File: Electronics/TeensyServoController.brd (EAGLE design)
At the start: 50.8 x 38.1 mm, 17 parts, among them U1 MK20DX128VLH5, U2 AP3211_SWITCHING_REGULATOR, U3 AP3211_SWITCHING_REGULATOR, U4 AP3211_SWITCHING_REGULATOR

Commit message: Continued Work on Teensy servo controller
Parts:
- added C1, C5, C6: 10nF, resistor:C0402
- added C10, C11, C12, C14, C15, C16, C7, C8: 0.1uF, resistor:C0402
- added C13, C9: 2.2uF, resistor:C0603
- added C2, C3, C4: 10uF, resistor:C0805
- added Q1: 16MHz, crystal:CTS406
- added R1, R3, R4: 349k, resistor:R0402
- added R2, R5, R6: 49.9k, resistor:R0402
- added R7, R8: 33, resistor:R0402
- added R9: 470, resistor:R0402
- added U5: (no value), SparkFun-Connectors:USB-AB-MICRO-SMD
- moved U$3 21.8 mm to (43.3, 30.7), turned to 270 degrees
- moved U1 8.47 mm to (32.3, 15.5), turned to 90 degrees
- moved U4 5.64 mm to (22.1, 30.0)
- moved U3 4.68 mm to (22.1, 18.8)
- moved U2 4.52 mm to (22.1, 7.62)
- moved L2 3.98 mm to (18.3, 19.1)
- moved L1 3.98 mm to (18.3, 7.87)
- moved L3 3.87 mm to (18.3, 30.2)
- moved JP9 3.56 mm to (1.52, 33.0)
- moved JP4 3.56 mm to (1.52, 16.3)
- moved JP5 3.56 mm to (1.52, 19.1)
- moved JP6 3.56 mm to (1.52, 21.8)
- moved JP1 3.56 mm to (1.52, 5.08)
- moved JP2 3.56 mm to (1.52, 7.87)
- moved JP3 3.56 mm to (1.52, 10.7)
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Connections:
- removed net N$8: U$3.17, U$3.25, U$3.47
- new net N$10: R7.1, U5.D-
- new net N$14: C1.2, U2.1
- new net N$15: R8.2, U1.5
- new net N$16: R4.1, R6.2, U4.3
- new net N$17: C5.2, U3.1
- new net N$18: R3.1, R5.2, U3.3
- new net N$19: C6.2, U4.1
- new net N$20: C6.1, L3.P$1, R4.2, U4.6
- new net N$21: C14.1, Q1.3, U1.32
- new net N$22: C15.1, Q1.1, U1.33
- new net N$23: C16.2, U1.8
- new net N$24: C9.1, R9.1, U1.13
- new net N$25: C7.2, C8.2, C9.2, U1.15, U1.16
- new net N$26: C7.1, U1.17
- new net N$27: C8.1, R9.2, U1.14
- new net N$30: U$3.8, U1.34
- new net N$31: C10.1, C11.1, C12.1, C13.1, U$3.42, U$3.43, U1.3, U1.30, U1.48, U1.7
- new net N$6: R1.1, R2.2, U2.3
- new net N$9: R8.1, U5.D+
- net GND: now also C10.2, C11.2, C12.2, C13.2, C14.2, C15.2, C16.1, C2.2, C3.2, C4.2, R2.1, R5.1, R6.1, U$3.17, U$3.25, U$3.47, U$3.5, U1.31, U1.4, U1.47, U2.2, U3.2, U4.2, U5.GND
- net N$1: now also U5.ID
- net N$11: now also C5.1, R3.2
- net N$12: now also R7.2, U1.6; no longer L3.P$1, U4.6
- net N$13: now also C1.1, R1.2
- net VCC: now also C2.1, C3.1, C4.1
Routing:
- net GND: track 0.00 -> 10.6 mm, vias 0 -> 25
- net N$13: track 0.00 -> 7.80 mm
- net N$11: track 0.00 -> 7.51 mm
- net N$20: track 0.00 -> 7.51 mm
- net VCC: track 0.00 -> 5.24 mm
- net N$6: track 0.00 -> 3.07 mm
- net N$18: track 0.00 -> 3.07 mm
- net N$16: track 0.00 -> 3.07 mm
- net N$17: track 0.00 -> 2.45 mm
- net N$14: track 0.00 -> 2.45 mm
- net N$19: track 0.00 -> 2.45 mm
- net N$9: track 0.00 -> 2.45 mm
- net N$10: track 0.00 -> 2.44 mm
- added copper zone on layer 1, net GND
- added copper zone on layer 16, net GND
- added copper zone on layer 1, net N$11
- added copper zone on layer 1, net N$13
- added copper zone on layer 1, net N$20
- added copper zone on layer 1, net SERVO_VDD-1
- added copper zone on layer 1, net SERVO_VDD-2
- added copper zone on layer 1, net SERVO_VDD-3

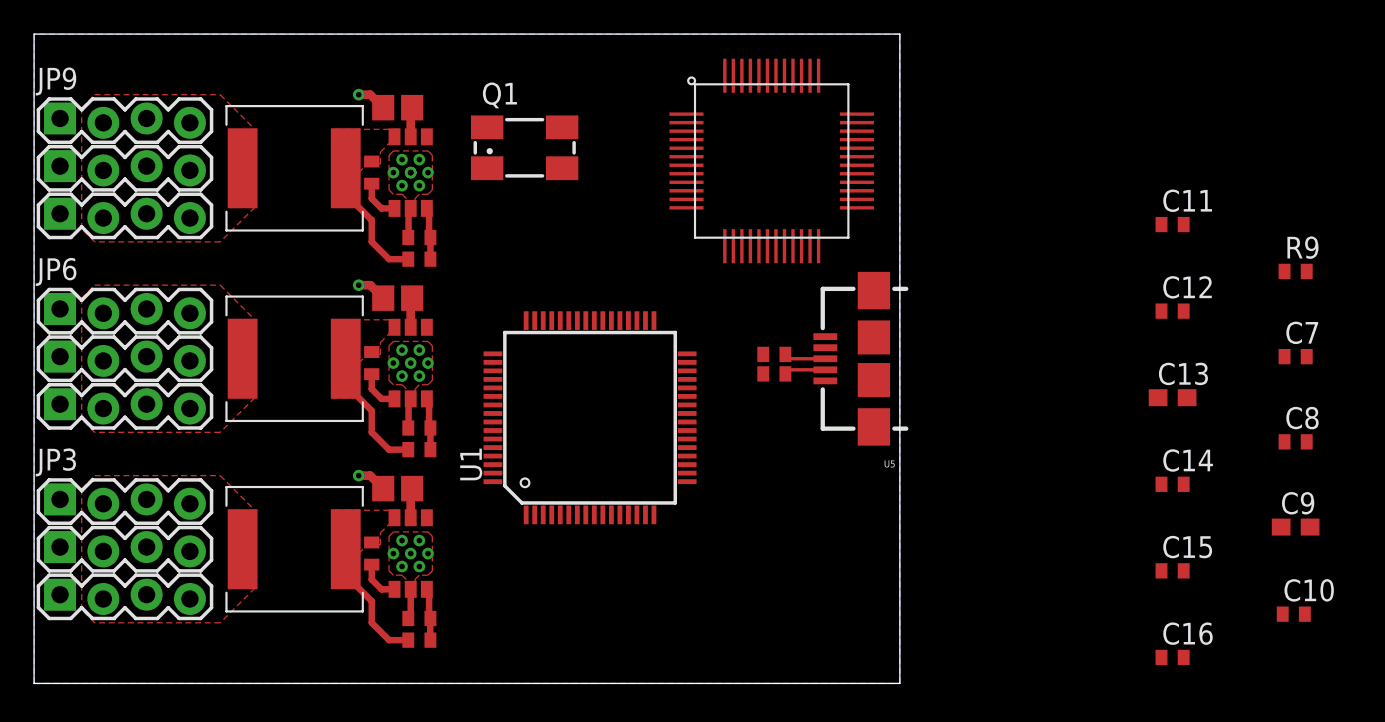
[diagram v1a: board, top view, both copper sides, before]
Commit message: Servo controller mostly done (no I sense)
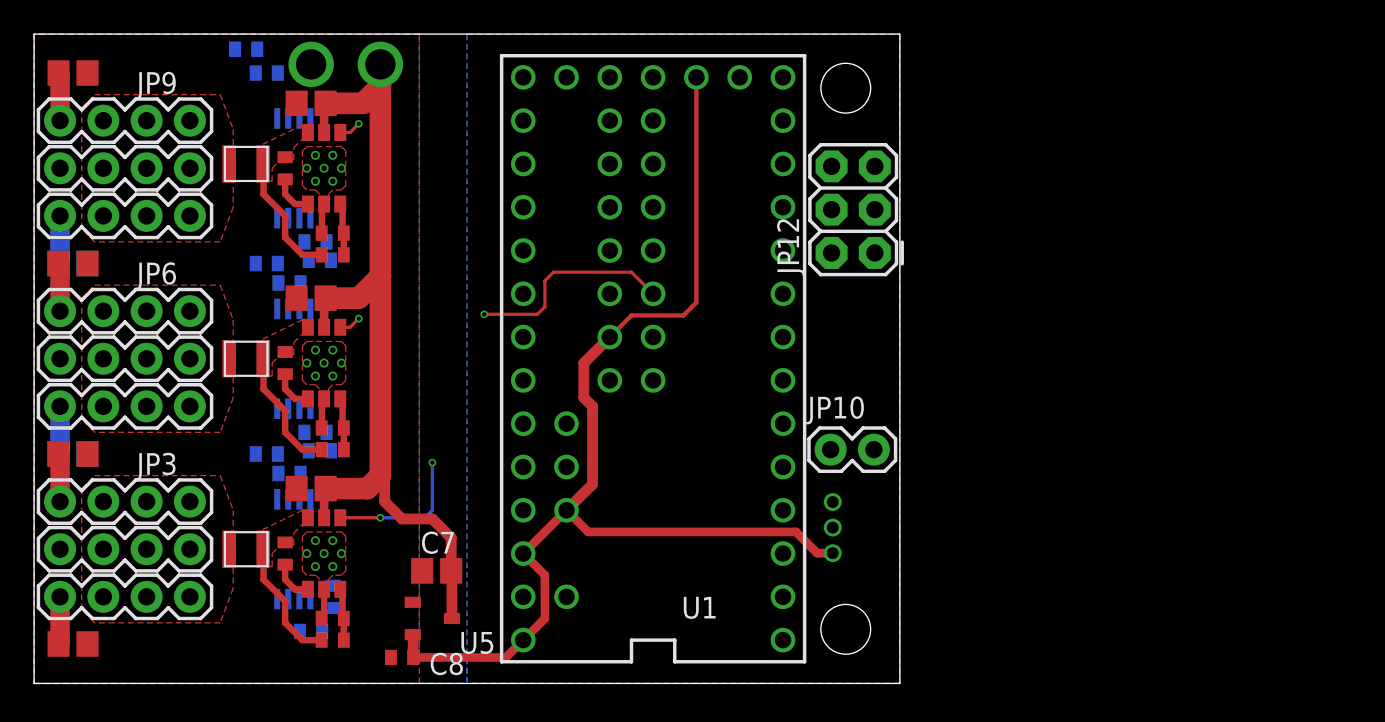
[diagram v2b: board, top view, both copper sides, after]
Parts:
- removed C10, C11, C12, C14, C15, C16: 0.1uF, resistor:C0402
- removed C13, C9: 2.2uF, resistor:C0603
- removed Q1: 16MHz, crystal:CTS406
- removed U$3: MINI54TAN, TeensyCustom:MINI54TAN
- added JP10: (no value), SparkFun-Connectors:1X02
- added JP11: 3-PIN_JST_ZH_PTH_CONNECTORRIGHT_ANGLE_PTH, My Parts:3-PIN_JST_ZH_CONNECTOR_TH
- added JP12: (no value), SparkFun-Connectors:2X3
- added R10, R11, R12, R17, R20, R23: 1k, resistor:R0402
- added R13, R14, R15, R18, R21, R24: 63.4k, resistor:R0402
- added R16, R19, R22: 0.1, resistor:R0805
- added U6, U7, U8: MCP6L02T-E/MS, linear:TSSOP8
- C7: value 0.1uF -> 10uF; device resistor:C0402 -> resistor:C0805
- JP1, JP2, JP3, JP4, JP5, JP6, JP7, JP8, JP9: device SparkFun-Connectors:1X04_LOCK -> SparkFun-Connectors:1X04
- L1, L2, L3: device SparkFun-Passives:CR75 -> inductors:1008
- R7, R8: value 33 -> 0.1; device resistor:R0402 -> resistor:R0805
- R9: value 470 -> 0.1; device resistor:R0402 -> resistor:R0805
- U1: value MK20DX128VLH5 -> TEENSY_3.1_ALLPINS; device TeensyCustom:MK20DX128VLH5 -> Teensy3.0:TEENSY_3.0_ALLPINS
- U2, U3, U4: value AP3211_SWITCHING_REGULATOR -> AP3211KTR-G1
- U5: value (none) -> AP2210N-3.3TRG1; device SparkFun-Connectors:USB-AB-MICRO-SMD -> My Parts:SOT23
- moved R9 72.5 mm to (2.29, 13.5), flipped to the bottom
- moved C8 53.9 mm to (21.6, 1.52), turned to 180 degrees
- moved C7 51.9 mm to (23.6, 6.60), turned to 180 degrees
- moved R7 44.1 mm to (2.29, 2.31)
- moved R8 41.6 mm to (2.29, 13.5)
- moved U5 30.1 mm to (23.4, 3.81), turned to 270 degrees
- moved L3 5.85 mm to (12.4, 30.5)
- moved L1 5.84 mm to (12.4, 7.87)
- moved L2 5.84 mm to (12.4, 19.1)
- moved U1 5.40 mm to (36.3, 19.1), turned to 180 degrees
- moved C6 5.09 mm to (14.7, 30.2)
- moved R4 5.09 mm to (17.5, 25.1)
- moved R6 5.09 mm to (17.5, 26.4)
- moved C4 5.09 mm to (16.3, 34.0)
- moved U4 5.09 mm to (17.0, 30.2)
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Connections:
- removed net N$1: U$3.38, U1.23, U5.ID
- removed net N$12: R7.2, U1.6
- removed net N$15: R8.2, U1.5
- removed net N$21: C14.1, Q1.3, U1.32
- removed net N$22: C15.1, Q1.1, U1.33
- removed net N$23: C16.2, U1.8
- removed net N$24: C9.1, R9.1, U1.13
- removed net N$25: C7.2, C8.2, C9.2, U1.15, U1.16
- removed net N$26: C7.1, U1.17
- removed net N$27: C8.1, R9.2, U1.14
- removed net N$30: U$3.8, U1.34
- removed net N$31: C10.1, C11.1, C12.1, C13.1, U$3.42, U$3.43, U1.3, U1.30, U1.48, U1.7
- removed net N$4: U$3.37, U1.24
- new net CS0: JP12.3, U1.10
- new net CURRENT-1: JP1.1, R7.2, U6.3
- new net CURRENT-3: JP3.1, R8.2, U6.5
- new net CURRENT-4: JP4.1, R9.2, U7.3
- new net CURRENT-6: JP6.1, R16.2, U7.5
- new net CURRENT-7: JP7.1, R19.2, U8.3
- new net CURRENT-9: JP9.1, R22.2, U8.5
- new net EN-1: U1.33, U2.4
- new net EN-2: U1.24, U3.4
- new net EN-3: U1.32, U4.4
- new net MISO/MOSI: JP12.5, U1.12
- new net MOSI/MISO: JP12.6, U1.11
- new net SAT-RX: JP10.1, JP11.P$3, U1.0
- new net SCLK: JP12.4, U1.13
- new net SENSE-1: R13.2, U6.1
- new net SENSE-3: R14.2, U6.7
- new net SENSE-4: R15.2, U7.1
- new net SENSE-6: R18.2, U7.7
- new net SENSE-7: R21.2, U8.1
- new net SENSE-9: R24.2, U8.7
- new net VBAT: U1.VBAT
- new net VDD: C8.1, JP11.P$1, U1.3.3V, U1.3.3V1, U1.3.3V2, U1.AREF, U1.VIN, U5.P$2, U6.8, U7.8, U8.8
- new net VUSB: U1.VUSB
- net ANALOG-1: now also U1.22/A8
- net ANALOG-2: now also U1.21/A7
- net ANALOG-3: now also U1.20/A6
- net ANALOG-4: now also U1.19/A5
- net ANALOG-5: now also U1.18/A4
- net ANALOG-6: now also U1.17/A3
- net ANALOG-7: now also U1.16/A2
- net ANALOG-8: now also U1.15/A1
- net ANALOG-9: now also U1.14/A0
- net GND: now also C7.2, C8.2, JP10.2, JP11.P$2, JP12.1, R10.2, R11.2, R12.2, R16.1, R17.2, R19.1, R20.2, R22.1, R23.2, R7.1, R8.1, R9.1, U1.AGND, U1.GND, U1.GND1, U1.GND2, U5.P$1, U6.4, U7.4, U8.4; no longer C10.2, C11.2, C12.2, C13.2, C14.2, C15.2, C16.1, JP1.1, JP3.1, JP4.1, JP6.1, JP7.1, JP9.1, U$3.17, U$3.25, U$3.47, U$3.5, U1.31, U1.4, U1.47, U5.GND
- net N$10: now also R20.1, R21.1, U8.2; no longer R7.1, U5.D-
- net N$2: now also R10.1, R13.1, U6.2; no longer U$3.33, U$3.34, U1.25
- net N$3: now also R11.1, R14.1, U6.6; no longer U$3.32, U1.22
- net N$5: now also R12.1, R15.1, U7.2; no longer U$3.10, U1.37
- net N$7: now also R17.1, R18.1, U7.6; no longer U$3.9, U1.38
- net N$9: now also R23.1, R24.1, U8.6; no longer R8.1, U5.D+
- net SERVO-1: now also U1.1
- net SERVO-2: now also U1.2
- net SERVO-3: now also U1.3
- net SERVO-4: now also U1.4
- net SERVO-5: now also U1.5
- net SERVO-6: now also U1.6
- net SERVO-7: now also U1.7
- net SERVO-8: now also U1.8
- net SERVO-9: now also U1.9
- net VCC: now also C7.1, JP12.2, U5.P$3
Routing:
- net VDD: track 0.00 -> 65.4 mm
- net SERVO-7: track 0.00 -> 48.7 mm
- net VCC: track 5.24 -> 52.3 mm, vias 0 -> 1
- net SERVO-4: track 0.00 -> 45.5 mm
- net SERVO-8: track 0.00 -> 45.3 mm
- net SERVO-5: track 0.00 -> 44.2 mm
- net SERVO-6: track 0.00 -> 44.1 mm
- net SERVO-1: track 0.00 -> 43.9 mm
- net SERVO-9: track 0.00 -> 43.1 mm
- net SERVO-2: track 0.00 -> 40.3 mm
- net SERVO-3: track 0.00 -> 39.2 mm
- net ANALOG-7: track 0.00 -> 27.5 mm
- net EN-1: track 0.00 -> 26.3 mm, vias 0 -> 2
- net ANALOG-1: track 0.00 -> 24.8 mm
- net ANALOG-4: track 0.00 -> 24.6 mm
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
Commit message: Electronics finalized and ordered
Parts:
- removed R21, R24: 63.4k, resistor:R0402
- removed R22: 0.1, resistor:R0805
- removed R23: 1k, resistor:R0402
- added C10, C11, C9: 22uF, resistor:C0603
- added C12: 10uF, resistor:C0805
- added C13, C14, C23, C24, C25, C26, C27, C28, C29, C30, C31, C32, C33, C34, C35, C36, C37, C38: 0.1uF, resistor:C0402
- added C15, C16: 0.1uF, resistor:C0603
- added C17, C18, C19, C20, C21, C22: 1uF, resistor:C0603
- added JP14, JP15: (no value), SparkFun-Connectors:1X02
- added LED1, LED2: (no value), SparkFun-LED:LED-0603
- added TP1, TP2, TP3, TP4, TP5, TP6: (no value), SparkFun-Passives:PAD.03X.03
- added U10, U11, U9: (no value), My Parts:SOT23-5
- added U12, U13: MIC5225, My Parts:SOT23-5
- C8: device resistor:C0402 -> resistor:C0603
- R10, R11, R12: value 1k -> 0.027; device resistor:R0402 -> resistor:R0603
- R13, R14, R15: value 63.4k -> (none)
- R16, R19: value 0.1 -> (none); device resistor:R0805 -> resistor:R0603
- R17: value 1k -> (none); device resistor:R0402 -> resistor:R0603
- R18: value 63.4k -> (none); device resistor:R0402 -> resistor:R0603
- R20: value 1k -> (none)
- R7, R8, R9: value 0.1 -> 0.027; device resistor:R0805 -> resistor:R0603
- U6, U7, U8: value MCP6L02T-E/MS -> (none); device linear:TSSOP8 -> My Parts:SOT23-5
- moved R19 41.1 mm to (41.7, 12.7), flipped to the top, turned to 90 degrees
- moved R16 40.2 mm to (39.4, 9.14)
- moved R17 33.4 mm to (41.7, 6.35), flipped to the top, turned to 90 degrees
- moved R13 33.2 mm to (46.5, 21.3), flipped to the top, turned to 180 degrees
- moved R20 29.8 mm to (46.5, 22.9), flipped to the top
- moved R18 25.7 mm to (39.4, 15.5), flipped to the top
- moved R14 25.2 mm to (24.1, 35.8), flipped to the top
- moved R15 23.6 mm to (24.1, 37.1), flipped to the top, turned to 0 degrees
- moved R12 21.4 mm to (11.2, 34.3), flipped to the top, turned to 90 degrees
- moved R10 20.7 mm to (11.2, 23.1), flipped to the top, turned to 90 degrees
- moved U8 18.1 mm to (24.1, 14.5), flipped to the top, turned to 90 degrees
- moved C7 13.7 mm to (36.6, 2.29), turned to 90 degrees
- moved U7 13.1 mm to (24.1, 9.40), flipped to the top, turned to 90 degrees
- moved R11 12.9 mm to (11.2, 26.2), flipped to the top, turned to 270 degrees
- moved C8 12.6 mm to (33.8, 4.83), turned to 0 degrees
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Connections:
- removed net N$2: R10.1, R13.1, U6.2
- removed net N$3: R11.1, R14.1, U6.6
- removed net N$5: R12.1, R15.1, U7.2
- removed net SENSE-1: R13.2, U6.1
- removed net SENSE-3: R14.2, U6.7
- removed net SENSE-4: R15.2, U7.1
- removed net SENSE-6: R18.2, U7.7
- removed net SENSE-7: R21.2, U8.1
- removed net SENSE-9: R24.2, U8.7
- new net AREF: C13.1, R16.2, U1.AREF, U12.5
- new net AREF2: C14.1, R18.2, U1.A13, U13.5
- new net BATT_SENSE: C29.1, R14.1, R15.2, U1.28
- new net I2C_SCL: JP14.1, U1.29
- new net I2C_SDA: JP15.2, U1.30
- new net N$1: LED1.A, R13.1
- new net N$8: R20.2, U1.25
- new net SERVO-1_VDD: C17.1, JP1.2, R7.2, U6.4
- new net SERVO-3_VDD: C18.1, JP3.2, R8.2, U7.4
- new net SERVO-4_VDD: C19.1, JP4.2, R9.2, U8.4
- new net SERVO-6_VDD: C20.1, JP6.2, R10.2, U9.4
- new net SERVO-7_VDD: C21.1, JP7.2, R11.2, U10.4
- new net SERVO-9_VDD: C22.1, JP9.2, R12.2, U11.4
- net ANALOG-1: now also C30.1
- net ANALOG-2: now also C31.1
- net ANALOG-3: now also C32.1
- net ANALOG-4: now also C33.1
- net ANALOG-5: now also C34.1
- net ANALOG-6: now also C35.1
- net ANALOG-7: now also C36.1
- net ANALOG-8: now also C37.1
- net ANALOG-9: now also C38.1
- net CURRENT-1: now also C23.1, TP1.P$1, U1.A10; no longer JP1.1, R7.2
- net CURRENT-3: now also C24.1, TP2.P$1, U1.A11, U7.3; no longer JP3.1, R8.2, U6.5
- net CURRENT-4: now also C25.1, TP3.P$1, U1.A12, U8.3; no longer JP4.1, R9.2, U7.3
- net CURRENT-6: now also C26.1, TP4.P$1, U1.31, U9.3; no longer JP6.1, R16.2, U7.5
- net CURRENT-7: now also C27.1, TP5.P$1, U1.26, U10.3; no longer JP7.1, R19.2, U8.3
- net CURRENT-9: now also C28.1, TP6.P$1, U1.27, U11.3; no longer JP9.1, R22.2, U8.5
- net GND: now also C10.2, C11.2, C12.2, C13.2, C14.2, C15.2, C16.2, C17.2, C18.2, C19.2, C20.2, C21.2, C22.2, C23.2, C24.2, C25.2, C26.2, C27.2, C28.2, C29.2, C30.2, C31.2, C32.2, C33.2, C34.2, C35.2, C36.2, C37.2, C38.2, C9.2, JP1.1, JP15.1, JP3.1, JP4.1, JP6.1, JP7.1, JP9.1, LED1.C, LED2.C, R15.1, R17.1, U10.1, U10.2, U11.1, U11.2, U12.2, U13.2, U6.1, U6.2, U7.1, U7.2, U8.1, U8.2, U9.1, U9.2; no longer R10.2, R11.2, R12.2, R16.1, R17.2, R20.2, R22.1, R23.2, R7.1, R8.1, R9.1, U6.4, U7.4, U8.4
- net N$10: now also LED2.A; no longer R21.1, U8.2
- net N$7: now also R16.1, R17.2, U12.4; no longer R17.1, R18.1, U7.6
- net N$9: now also R18.1, R19.2, U13.4; no longer R23.1, R24.1, U8.6
- net SERVO_VDD-1: now also C11.1, R7.1, R8.1, U6.5, U7.5; no longer JP1.2, JP3.2
- net SERVO_VDD-2: now also C10.1, R10.1, R9.1, U8.5, U9.5; no longer JP4.2, JP6.2
- net SERVO_VDD-3: now also C9.1, R11.1, R12.1, U10.5, U11.5; no longer JP7.2, JP9.2
- net VCC: now also C12.1, C15.1, C16.1, R14.2, U12.1, U12.3, U13.1, U13.3; no longer JP12.2
- net VDD: now also JP12.2, JP14.2, R13.2; no longer U1.AREF, U6.8, U7.8, U8.8
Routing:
- net VCC: track 52.3 -> 101.7 mm
- net GND: track 5.37 -> 39.6 mm, vias 22 -> 131
- net SERVO_VDD-3: track 0.00 -> 27.0 mm, vias 0 -> 4
- net SERVO-1_VDD: track 0.00 -> 27.0 mm, vias 0 -> 2
- net SERVO-4_VDD: track 0.00 -> 26.9 mm, vias 0 -> 2
- net SERVO-7_VDD: track 0.00 -> 26.9 mm, vias 0 -> 2
- net VDD: track 65.4 -> 92.3 mm
- net SERVO_VDD-2: track 0.00 -> 26.9 mm, vias 0 -> 4
- net SERVO_VDD-1: track 0.00 -> 26.3 mm, vias 0 -> 4
- net I2C_SCL: track 0.00 -> 25.6 mm
- net SERVO-6_VDD: track 0.00 -> 25.0 mm, vias 0 -> 2
- net I2C_SDA: track 0.00 -> 24.8 mm
- net SERVO-3_VDD: track 0.00 -> 24.8 mm, vias 0 -> 2
- net SERVO-9_VDD: track 0.00 -> 24.8 mm, vias 0 -> 2
- net CURRENT-4: track 2.83 -> 23.3 mm, vias 0 -> 1
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- added copper zone on layer 2, net GND
- added copper zone on layer 1, net N$2
- added copper zone on layer 1, net N$3
- added copper zone on layer 1, net N$4
- added copper zone on layer 1, net N$5
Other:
- board text added: "+"
- board text added: "-"
- board text added: "1"
- board text added: "3"
- board text added: "4"
- board text added: "6"
- board text added: "7"
- board text added: "9"
- board text added: "L1"
- board text added: "L2"
- board text added: "L3"

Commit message: Finalized values for most components on PCBs
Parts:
- LED1: value (none) -> red
- LED2: value (none) -> blue
- R14: value (none) -> 150k
- R15: value (none) -> 49.9k
- R17, R19: value (none) -> 255k
- R20: value (none) -> 91
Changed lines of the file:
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@@
 <setting verticaltext="up"/>
 </settings>
-<grid distance="0.01" unitdist="inch" unit="inch" style="lines" multiple="1" display="yes" altdistance="0.0025" altunitdist="inch" altunit="inch"/>
+<grid distance="0.25" unitdist="mm" unit="mm" style="lines" multiple="1" display="yes" altdistance="0.05" altunitdist="mm" altunit="mm"/>
 <layers>
 <layer number="1" name="Top" color="4" fill="1" visible="yes" active="yes"/>
@@
 <attribute name="VALUE" x="24.3205" y="30.5435" size="0.4064" layer="27" rot="R90"/>
 </element>
-<element name="LED1" library="SparkFun-LED" package="LED-0603" value="" x="49.022" y="21.336" smashed="yes" rot="R270">
+<element name="LED1" library="SparkFun-LED" package="LED-0603" value="red" x="49.022" y="21.336" smashed="yes" rot="R270">
 <attribute name="VALUE" x="48.006" y="20.2565" size="0.4064" layer="27"/>
 </element>
@@
 <attribute name="VALUE" x="47.117" y="23.368" size="1.27" layer="27" rot="R180"/>
 </element>
-<element name="R15" library="resistor" package="R0402" value="" x="24.13" y="37.084" smashed="yes">
+<element name="R15" library="resistor" package="R0402" value="49.9k" x="24.13" y="37.084" smashed="yes">
 <attribute name="NAME" x="25.273" y="36.83" size="0.762" layer="25" ratio="15"/>
 <attribute name="VALUE" x="23.495" y="35.052" size="1.27" layer="27"/>
 </element>
-<element name="R14" library="resistor" package="R0402" value="" x="24.13" y="35.814" smashed="yes" rot="R180">
+<element name="R14" library="resistor" package="R0402" value="150k" x="24.13" y="35.814" smashed="yes" rot="R180">
 <attribute name="NAME" x="25.273" y="35.306" size="0.762" layer="25" ratio="15"/>
 <attribute name="VALUE" x="24.765" y="37.846" size="1.27" layer="27" rot="R180"/>
@@
 <attribute name="VALUE" x="40.259" y="11.176" size="1.27" layer="27" rot="R180"/>
 </element>
-<element name="R17" library="resistor" package="R0603" value="" x="41.656" y="6.35" smashed="yes" rot="R90">
+<element name="R17" library="resistor" package="R0603" value="255k" x="41.656" y="6.35" smashed="yes" rot="R90">
 <attribute name="NAME" x="42.545" y="7.493" size="0.635" layer="25" ratio="15" rot="R270"/>
 <attribute name="VALUE" x="43.688" y="5.461" size="1.27" layer="27" rot="R90"/>
@@
 <attribute name="VALUE" x="40.259" y="17.526" size="1.27" layer="27" rot="R180"/>
 </element>
-<element name="R19" library="resistor" package="R0603" value="" x="41.656" y="12.7" smashed="yes" rot="R90">
+<element name="R19" library="resistor" package="R0603" value="255k" x="41.656" y="12.7" smashed="yes" rot="R90">
 <attribute name="NAME" x="42.037" y="14.351" size="0.635" layer="25" ratio="15" rot="R90"/>
 <attribute name="VALUE" x="43.688" y="11.811" size="1.27" layer="27" rot="R90"/>
@@
 <attribute name="NAME" x="41.021" y="2.54" size="0.762" layer="25" ratio="15"/>
 </element>
-<element name="LED2" library="SparkFun-LED" package="LED-0603" value="" x="49.022" y="22.86" smashed="yes" rot="R270">
+<element name="LED2" library="SparkFun-LED" package="LED-0603" value="blue" x="49.022" y="22.86" smashed="yes" rot="R270">
 <attribute name="VALUE" x="48.006" y="21.7805" size="0.4064" layer="27"/>
 </element>
-<element name="R20" library="resistor" package="R0402" value="" x="46.482" y="22.86" smashed="yes" rot="R180">
+<element name="R20" library="resistor" package="R0402" value="91" x="46.482" y="22.86" smashed="yes" rot="R180">
 <attribute name="VALUE" x="47.117" y="24.892" size="1.27" layer="27" rot="R180"/>
 </element>
